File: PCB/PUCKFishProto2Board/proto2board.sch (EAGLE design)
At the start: 7 parts, among them U1 MS583730BA01-50, U2 ZXCT1107SA-7

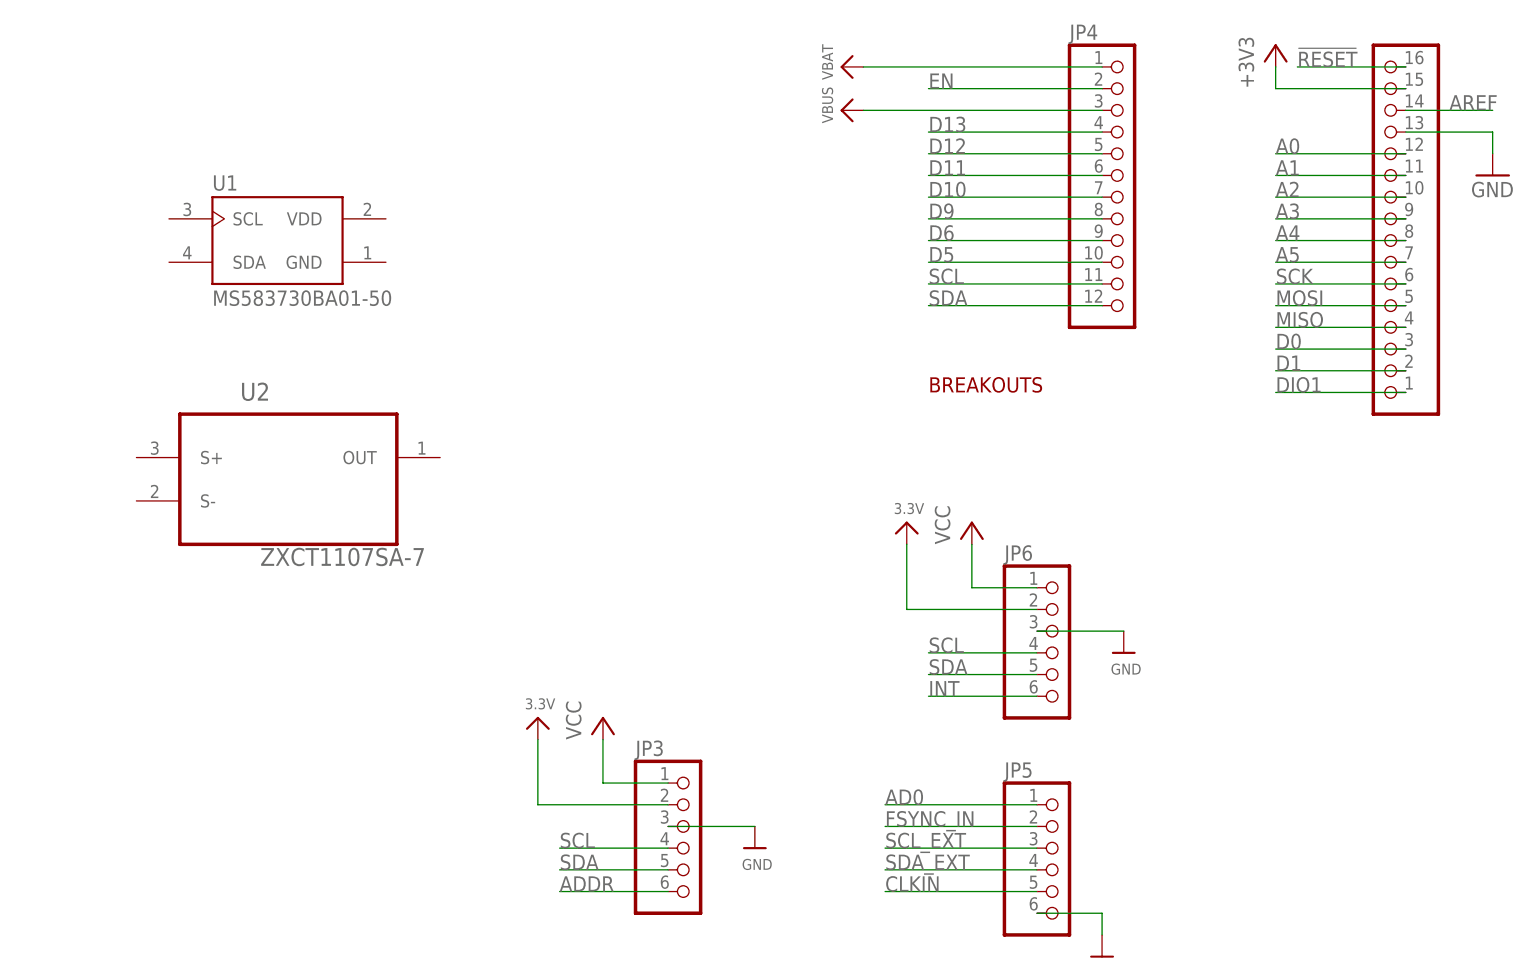
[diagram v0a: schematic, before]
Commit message: Schematic done except salinity sensor
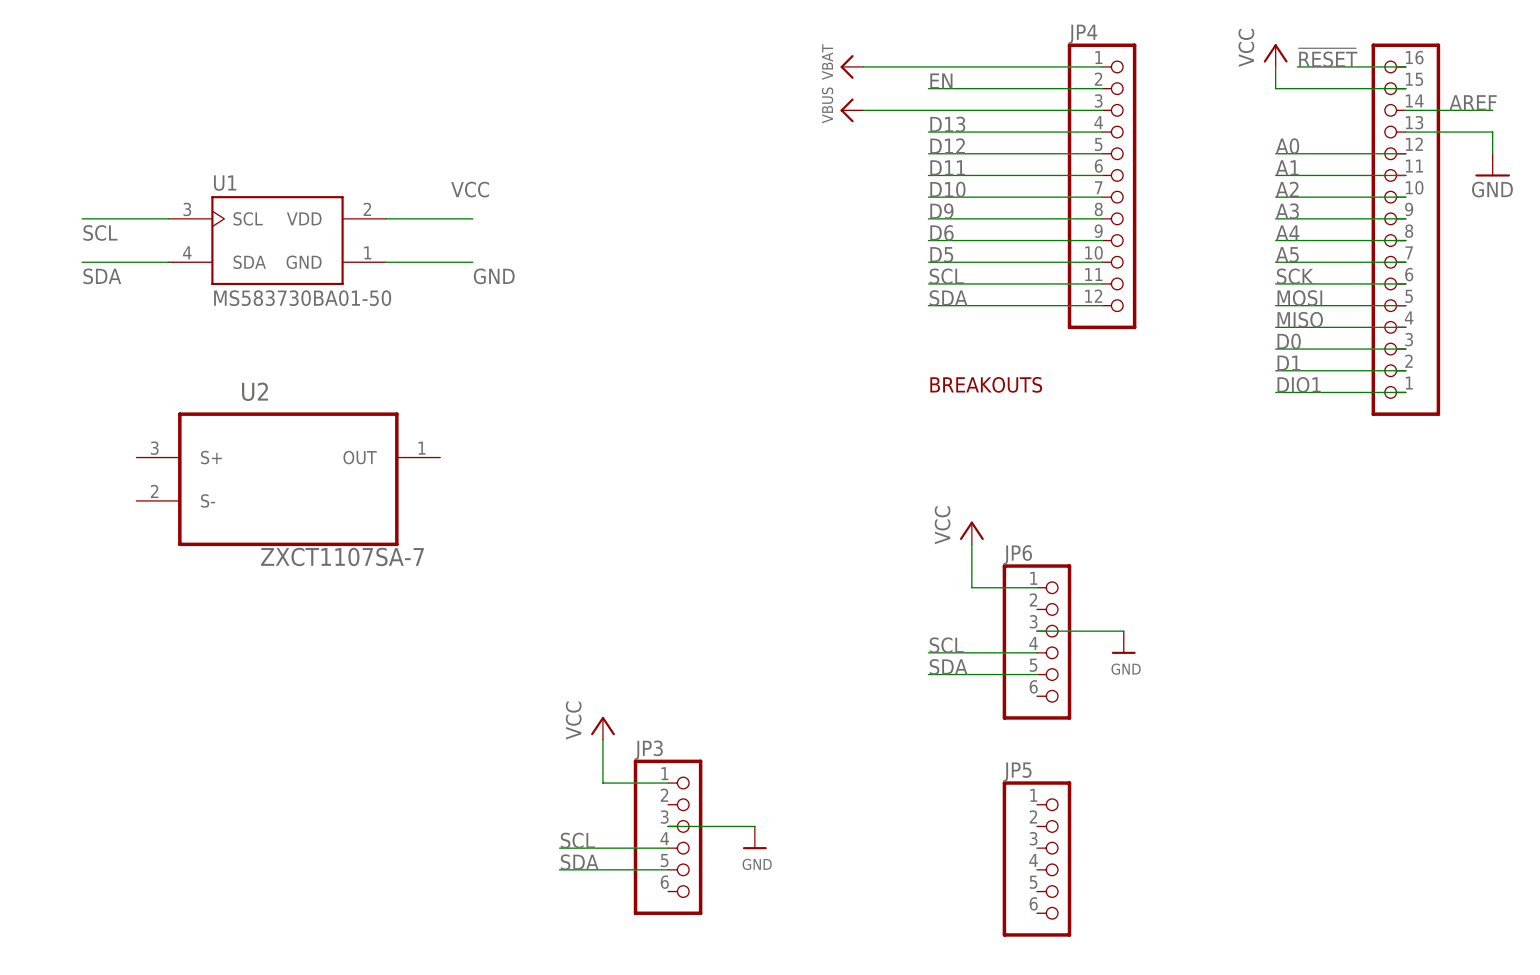
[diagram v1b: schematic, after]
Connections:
- removed net +3V3: JP2.15
- removed net 3.3V: JP3.2, JP6.2
- removed net AD0: JP5.1
- removed net ADDR: JP3.6
- removed net CLKIN: JP5.5
- removed net FSYNC_IN: JP5.2
- removed net INT: JP6.6
- removed net SCL_EXT: JP5.3
- removed net SDA_EXT: JP5.4
- net GND: now also U1.GND; no longer JP5.6
- net SCL: now also U1.SCL
- net SDA: now also U1.SDA
- net VCC: now also JP2.15, U1.VDD
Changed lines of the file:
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@@
 <part name="U$2" library="microbuilder" deviceset="VBAT" device=""/>
 <part name="JP2" library="microbuilder" deviceset="HEADER-1X16" device="ROUND"/>
-<part name="+3V2" library="supply1" deviceset="+3V3" device=""/>
 <part name="GND1" library="supply1" deviceset="GND" device=""/>
 <part name="JP4" library="microbuilder" deviceset="HEADER-1X12" device=""/>
 <part name="JP5" library="microbuilder" deviceset="HEADER-1X6" device="ROUND"/>
-<part name="U$3" library="microbuilder" deviceset="GND" device=""/>
 <part name="U$4" library="microbuilder" deviceset="GND" device=""/>
-<part name="U$5" library="microbuilder" deviceset="3.3V" device=""/>
 <part name="JP6" library="microbuilder" deviceset="HEADER-1X6" device="70MIL"/>
 <part name="P+1" library="supply1" library_urn="urn:adsk.eagle:library:371" deviceset="VCC" device=""/>
 <part name="U$9" library="microbuilder" deviceset="GND" device=""/>
-<part name="U$11" library="microbuilder" deviceset="3.3V" device=""/>
 <part name="JP3" library="microbuilder" deviceset="HEADER-1X6" device="70MIL"/>
 <part name="P+2" library="supply1" library_urn="urn:adsk.eagle:library:371" deviceset="VCC" device=""/>
+<part name="P+3" library="supply1" library_urn="urn:adsk.eagle:library:371" deviceset="VCC" device=""/>
 </parts>
 <sheets>
@@
 <attribute name="VALUE" x="273.05" y="81.28" size="1.778" layer="96" rot="R180"/>
 </instance>
-<instance part="+3V2" gate="G$1" x="254" y="78.74" smashed="yes">
-<attribute name="VALUE" x="251.46" y="73.66" size="1.778" layer="96" rot="R90"/>
-</instance>
 <instance part="GND1" gate="1" x="279.4" y="63.5" smashed="yes">
 <attribute name="VALUE" x="276.86" y="60.96" size="1.778" layer="96"/>
@@
 <attribute name="VALUE" x="234.696" y="5.08" size="1.27" layer="96"/>
 </instance>
-<instance part="U$5" gate="G$1" x="210.82" y="22.86" smashed="yes">
-<attribute name="VALUE" x="209.296" y="23.876" size="1.27" layer="96"/>
-</instance>
 <instance part="JP6" gate="A" x="228.6" y="7.62" smashed="yes">
 <attribute name="NAME" x="222.25" y="18.415" size="1.778" layer="95"/>
@@
 <attribute name="VALUE" x="222.25" y="-27.94" size="1.778" layer="96"/>
 </instance>
-<instance part="U$3" gate="G$1" x="233.68" y="-27.94" smashed="yes"/>
 <instance part="U$9" gate="G$1" x="193.04" y="-15.24" smashed="yes">
 <attribute name="VALUE" x="191.516" y="-17.78" size="1.27" layer="96"/>
-</instance>
-<instance part="U$11" gate="G$1" x="167.64" y="0" smashed="yes">
-<attribute name="VALUE" x="166.116" y="1.016" size="1.27" layer="96"/>
 </instance>
 <instance part="JP3" gate="A" x="185.42" y="-15.24" smashed="yes">
@@
 <instance part="P+2" gate="VCC" x="175.26" y="0" smashed="yes">
 <attribute name="VALUE" x="172.72" y="-2.54" size="1.778" layer="96" rot="R90"/>
+</instance>
+<instance part="P+3" gate="VCC" x="254" y="78.74" smashed="yes">
+<attribute name="VALUE" x="251.46" y="76.2" size="1.778" layer="96" rot="R90"/>
 </instance>
 </instances>
@@
 </segment>
 <segment>
-<pinref part="JP5" gate="A" pin="6"/>
-<wire x1="226.06" y1="-22.86" x2="233.68" y2="-22.86" width="0.1524" layer="91"/>
-<pinref part="U$3" gate="G$1" pin="GND"/>
-<wire x1="233.68" y1="-22.86" x2="233.68" y2="-25.4" width="0.1524" layer="91"/>
-</segment>
-<segment>
 <pinref part="U$9" gate="G$1" pin="GND"/>
 <wire x1="182.88" y1="-12.7" x2="193.04" y2="-12.7" width="0.1524" layer="91"/>
 <pinref part="JP3" gate="A" pin="3"/>
 </segment>
+<segment>
+<pinref part="U1" gate="G$1" pin="GND"/>
+<wire x1="149.86" y1="53.34" x2="160.02" y2="53.34" width="0.1524" layer="91"/>
+<label x="160.02" y="50.8" size="1.778" layer="95"/>
+</segment>
 </net>
 <net name="MOSI" class="0">
@@
 </segment>
 </net>
-<net name="+3V3" class="0">
-<segment>
-<pinref part="+3V2" gate="G$1" pin="+3V3"/>
-<wire x1="254" y1="76.2" x2="254" y2="73.66" width="0.1524" layer="91"/>
-<pinref part="JP2" gate="A" pin="15"/>
-<wire x1="254" y1="73.66" x2="269.24" y2="73.66" width="0.1524" layer="91"/>
-</segment>
-</net>
 <net name="VBUS" class="0">
 <segment>
@@
 <pinref part="JP3" gate="A" pin="4"/>
 </segment>
+<segment>
+<pinref part="U1" gate="G$1" pin="SCL"/>
+<wire x1="124.46" y1="58.42" x2="114.3" y2="58.42" width="0.1524" layer="91"/>
+<label x="114.3" y="55.88" size="1.778" layer="95"/>
+</segment>
 </net>
 <net name="SDA" class="0">
@@
 <label x="170.18" y="-17.78" size="1.778" layer="95"/>
 <pinref part="JP3" gate="A" pin="5"/>
+</segment>
+<segment>
+<pinref part="U1" gate="G$1" pin="SDA"/>
+<wire x1="124.46" y1="53.34" x2="114.3" y2="53.34" width="0.1524" layer="91"/>
+<label x="114.3" y="50.8" size="1.778" layer="95"/>
 </segment>
 </net>
@@
 <pinref part="P+2" gate="VCC" pin="VCC"/>
 </segment>
-</net>
-<net name="3.3V" class="0">
-<segment>
-<wire x1="226.06" y1="12.7" x2="210.82" y2="12.7" width="0.1524" layer="91"/>
-<wire x1="210.82" y1="12.7" x2="210.82" y2="20.32" width="0.1524" layer="91"/>
-<pinref part="U$5" gate="G$1" pin="3.3V"/>
-<pinref part="JP6" gate="A" pin="2"/>
-</segment>
-<segment>
-<wire x1="182.88" y1="-10.16" x2="167.64" y2="-10.16" width="0.1524" layer="91"/>
-<wire x1="167.64" y1="-10.16" x2="167.64" y2="-2.54" width="0.1524" layer="91"/>
-<pinref part="U$11" gate="G$1" pin="3.3V"/>
-<pinref part="JP3" gate="A" pin="2"/>
-</segment>
-</net>
-<net name="INT" class="0">
-<segment>
-<pinref part="JP6" gate="A" pin="6"/>
-<wire x1="226.06" y1="2.54" x2="213.36" y2="2.54" width="0.1524" layer="91"/>
-<label x="213.36" y="2.54" size="1.778" layer="95"/>
-</segment>
-</net>
-<net name="FSYNC_IN" class="0">
-<segment>
-<wire x1="208.28" y1="-12.7" x2="226.06" y2="-12.7" width="0.1524" layer="91"/>
-<label x="208.28" y="-12.7" size="1.778" layer="95"/>
-<pinref part="JP5" gate="A" pin="2"/>
-</segment>
-</net>
-<net name="CLKIN" class="0">
-<segment>
-<wire x1="226.06" y1="-20.32" x2="208.28" y2="-20.32" width="0.1524" layer="91"/>
-<label x="208.28" y="-20.32" size="1.778" layer="95"/>
-<pinref part="JP5" gate="A" pin="5"/>
-</segment>
-</net>
-<net name="SDA_EXT" class="0">
-<segment>
-<wire x1="208.28" y1="-17.78" x2="226.06" y2="-17.78" width="0.1524" layer="91"/>
-<label x="208.28" y="-17.78" size="1.778" layer="95"/>
-<pinref part="JP5" gate="A" pin="4"/>
-</segment>
-</net>
-<net name="SCL_EXT" class="0">
-<segment>
-<wire x1="208.28" y1="-15.24" x2="226.06" y2="-15.24" width="0.1524" layer="91"/>
-<label x="208.28" y="-15.24" size="1.778" layer="95"/>
-<pinref part="JP5" gate="A" pin="3"/>
-</segment>
-</net>
-<net name="AD0" class="0">
-<segment>
-<wire x1="208.28" y1="-10.16" x2="226.06" y2="-10.16" width="0.1524" layer="91"/>
-<label x="208.28" y="-10.16" size="1.778" layer="95"/>
-<pinref part="JP5" gate="A" pin="1"/>
-</segment>
-</net>
-<net name="ADDR" class="0">
-<segment>
-<pinref part="JP3" gate="A" pin="6"/>
-<wire x1="182.88" y1="-20.32" x2="170.18" y2="-20.32" width="0.1524" layer="91"/>
-<label x="170.18" y="-20.32" size="1.778" layer="95"/>
-</segment>
-</net>
+<segment>
+<wire x1="254" y1="76.2" x2="254" y2="73.66" width="0.1524" layer="91"/>
+<pinref part="JP2" gate="A" pin="15"/>
+<wire x1="254" y1="73.66" x2="269.24" y2="73.66" width="0.1524" layer="91"/>
+<pinref part="P+3" gate="VCC" pin="VCC"/>
+</segment>
+<segment>
+<pinref part="U1" gate="G$1" pin="VDD"/>
+<wire x1="149.86" y1="58.42" x2="160.02" y2="58.42" width="0.1524" layer="91"/>
+<label x="157.48" y="60.96" size="1.778" layer="95"/>
+</segment>
+</net>

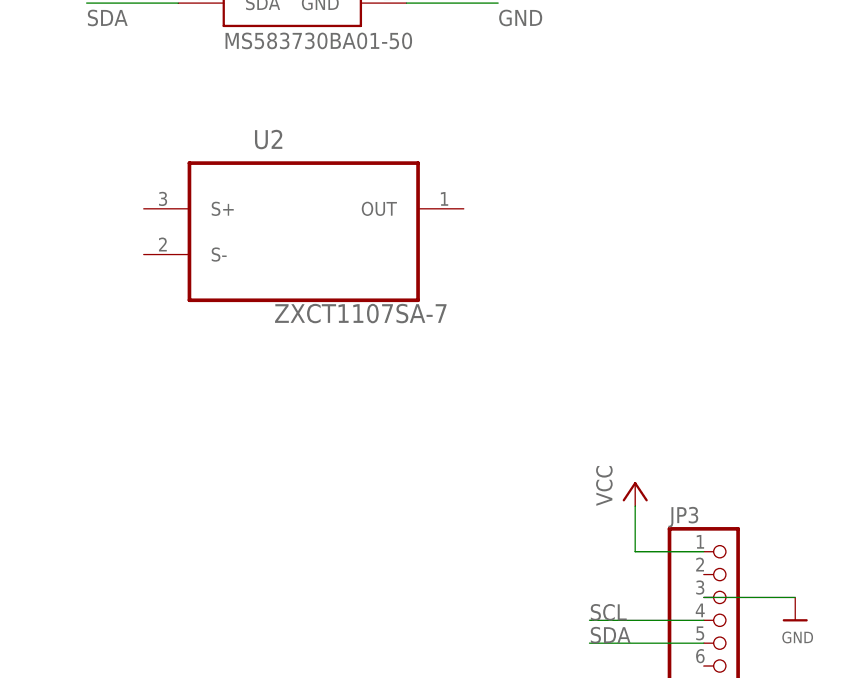
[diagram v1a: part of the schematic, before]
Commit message: Salinity incorporated into sch better now
Resistors added, needs proofreading
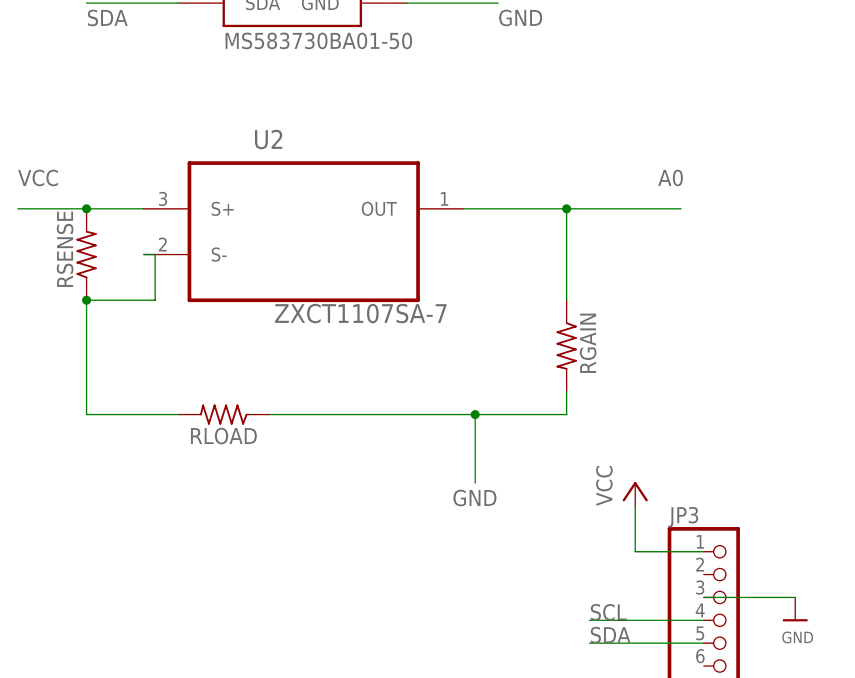
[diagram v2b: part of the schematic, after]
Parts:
- added RGAIN, RLOAD, RSENSE: (no value), rcl:R-US_0204/7
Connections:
- new net N$2: RLOAD.2, RSENSE.1, U2.S-
- net A0: now also RGAIN.1, U2.OUT
- net GND: now also RGAIN.2, RLOAD.1
- net VCC: now also RSENSE.2, U2.S+
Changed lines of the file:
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@@
 <part name="P+2" library="supply1" library_urn="urn:adsk.eagle:library:371" deviceset="VCC" device=""/>
 <part name="P+3" library="supply1" library_urn="urn:adsk.eagle:library:371" deviceset="VCC" device=""/>
+<part name="RSENSE" library="rcl" library_urn="urn:adsk.eagle:library:334" deviceset="R-US_" device="0204/7" package3d_urn="urn:adsk.eagle:package:23498/2"/>
+<part name="RLOAD" library="rcl" library_urn="urn:adsk.eagle:library:334" deviceset="R-US_" device="0204/7" package3d_urn="urn:adsk.eagle:package:23498/2"/>
+<part name="RGAIN" library="rcl" library_urn="urn:adsk.eagle:library:334" deviceset="R-US_" device="0204/7" package3d_urn="urn:adsk.eagle:package:23498/2"/>
 </parts>
 <sheets>
@@
 <attribute name="VALUE" x="251.46" y="76.2" size="1.778" layer="96" rot="R90"/>
 </instance>
+<instance part="RSENSE" gate="G$1" x="114.3" y="25.4" smashed="yes" rot="R90">
+<attribute name="NAME" x="112.8014" y="21.59" size="1.778" layer="95" rot="R90"/>
+<attribute name="VALUE" x="117.602" y="21.59" size="1.778" layer="96" rot="R90"/>
+</instance>
+<instance part="RLOAD" gate="G$1" x="129.54" y="7.62" smashed="yes" rot="R180">
+<attribute name="NAME" x="133.35" y="6.1214" size="1.778" layer="95" rot="R180"/>
+<attribute name="VALUE" x="133.35" y="10.922" size="1.778" layer="96" rot="R180"/>
+</instance>
+<instance part="RGAIN" gate="G$1" x="167.64" y="15.24" smashed="yes" rot="R270">
+<attribute name="NAME" x="169.1386" y="19.05" size="1.778" layer="95" rot="R270"/>
+<attribute name="VALUE" x="164.338" y="19.05" size="1.778" layer="96" rot="R270"/>
+</instance>
 </instances>
 <busses>
@@
 <label x="160.02" y="50.8" size="1.778" layer="95"/>
 </segment>
+<segment>
+<pinref part="RLOAD" gate="G$1" pin="1"/>
+<wire x1="134.62" y1="7.62" x2="157.48" y2="7.62" width="0.1524" layer="91"/>
+<pinref part="RGAIN" gate="G$1" pin="2"/>
+<wire x1="157.48" y1="7.62" x2="167.64" y2="7.62" width="0.1524" layer="91"/>
+<wire x1="167.64" y1="7.62" x2="167.64" y2="10.16" width="0.1524" layer="91"/>
+<wire x1="157.48" y1="7.62" x2="157.48" y2="0" width="0.1524" layer="91"/>
+<junction x="157.48" y="7.62"/>
+<label x="154.94" y="-2.54" size="1.778" layer="95"/>
+</segment>
 </net>
 <net name="MOSI" class="0">
@@
 <pinref part="JP2" gate="A" pin="12"/>
 <label x="254" y="66.04" size="1.778" layer="95"/>
+</segment>
+<segment>
+<pinref part="U2" gate="A" pin="OUT"/>
+<wire x1="156.21" y1="30.48" x2="167.64" y2="30.48" width="0.1524" layer="91"/>
+<wire x1="167.64" y1="30.48" x2="180.34" y2="30.48" width="0.1524" layer="91"/>
+<wire x1="167.64" y1="30.48" x2="167.64" y2="20.32" width="0.1524" layer="91"/>
+<junction x="167.64" y="30.48"/>
+<pinref part="RGAIN" gate="G$1" pin="1"/>
+<label x="177.8" y="33.02" size="1.778" layer="95"/>
 </segment>
 </net>
@@
 <wire x1="149.86" y1="58.42" x2="160.02" y2="58.42" width="0.1524" layer="91"/>
 <label x="157.48" y="60.96" size="1.778" layer="95"/>
+</segment>
+<segment>
+<pinref part="U2" gate="A" pin="S+"/>
+<wire x1="120.65" y1="30.48" x2="114.3" y2="30.48" width="0.1524" layer="91"/>
+<label x="106.68" y="33.02" size="1.778" layer="95"/>
+<pinref part="RSENSE" gate="G$1" pin="2"/>
+<wire x1="114.3" y1="30.48" x2="106.68" y2="30.48" width="0.1524" layer="91"/>
+<junction x="114.3" y="30.48"/>
+</segment>
+</net>
+<net name="N$2" class="0">
+<segment>
+<pinref part="RSENSE" gate="G$1" pin="1"/>
+<wire x1="114.3" y1="20.32" x2="121.92" y2="20.32" width="0.1524" layer="91"/>
+<pinref part="U2" gate="A" pin="S-"/>
+<wire x1="121.92" y1="20.32" x2="121.92" y2="25.4" width="0.1524" layer="91"/>
+<wire x1="121.92" y1="25.4" x2="120.65" y2="25.4" width="0.1524" layer="91"/>
+<wire x1="114.3" y1="20.32" x2="114.3" y2="7.62" width="0.1524" layer="91"/>
+<junction x="114.3" y="20.32"/>
+<wire x1="114.3" y1="7.62" x2="124.46" y2="7.62" width="0.1524" layer="91"/>
+<pinref part="RLOAD" gate="G$1" pin="2"/>
 </segment>
 </net>
@@
 will not be understood (or retained) with this version.
 </note>
+<note version="8.3" severity="warning">
+Since Version 8.3, EAGLE supports the association of 3D packages
+with devices in libraries, schematics, and board files. Those 3D
+packages will not be understood (or retained) with this version.
+</note>
+<note version="8.4" severity="warning">
+Since Version 8.4, EAGLE supports properties for SPICE simulation.
+Probes in schematics and SPICE mapping objects found in parts and library devices
+will not be understood with this version. Update EAGLE to the latest version
+for full support of SPICE simulation.
+</note>
 </compatibility>
